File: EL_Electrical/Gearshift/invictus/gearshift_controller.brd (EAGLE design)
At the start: 69.5 x 68.4 mm, 69 parts, among them IC1 MCP2562-E_SN, IC2 MCP2515-I_SO, Q1 BSS138, Q10 BSS138, Q2 BSS138, Q3 BSS138, Q4 BSS138, Q5 BSS138, Q6 BSS138, Q8 BSS138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

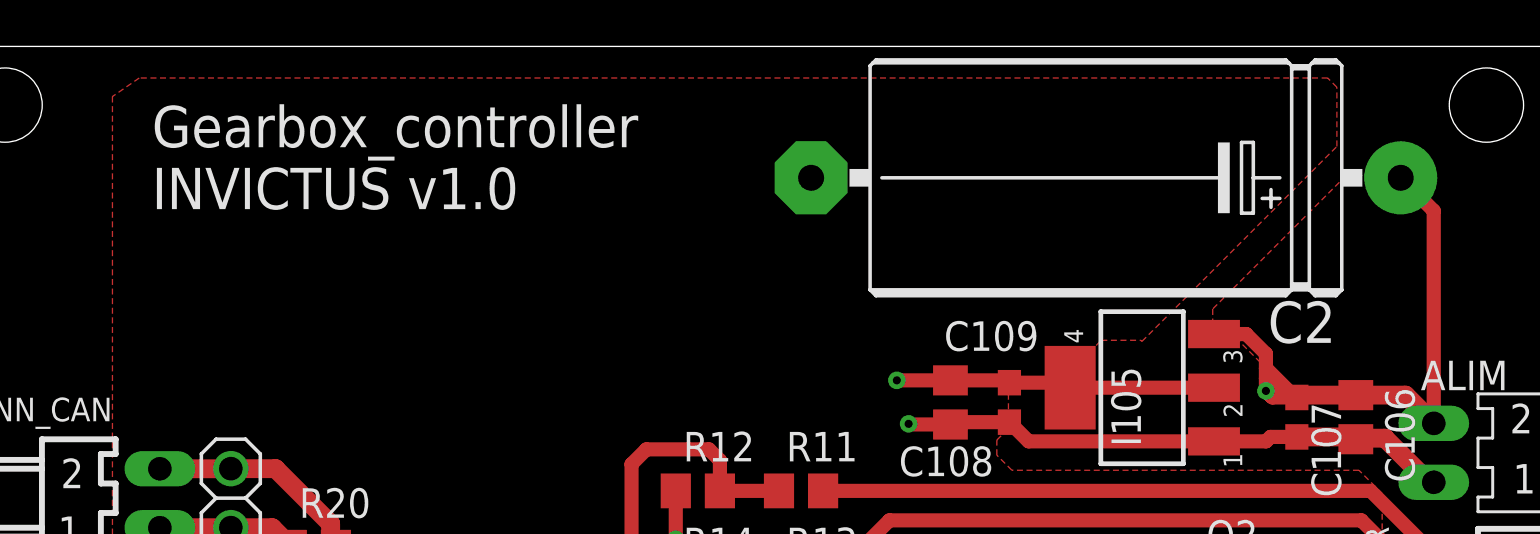
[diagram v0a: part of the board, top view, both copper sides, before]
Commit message: Delete useless resistors (Dashboard_controller)
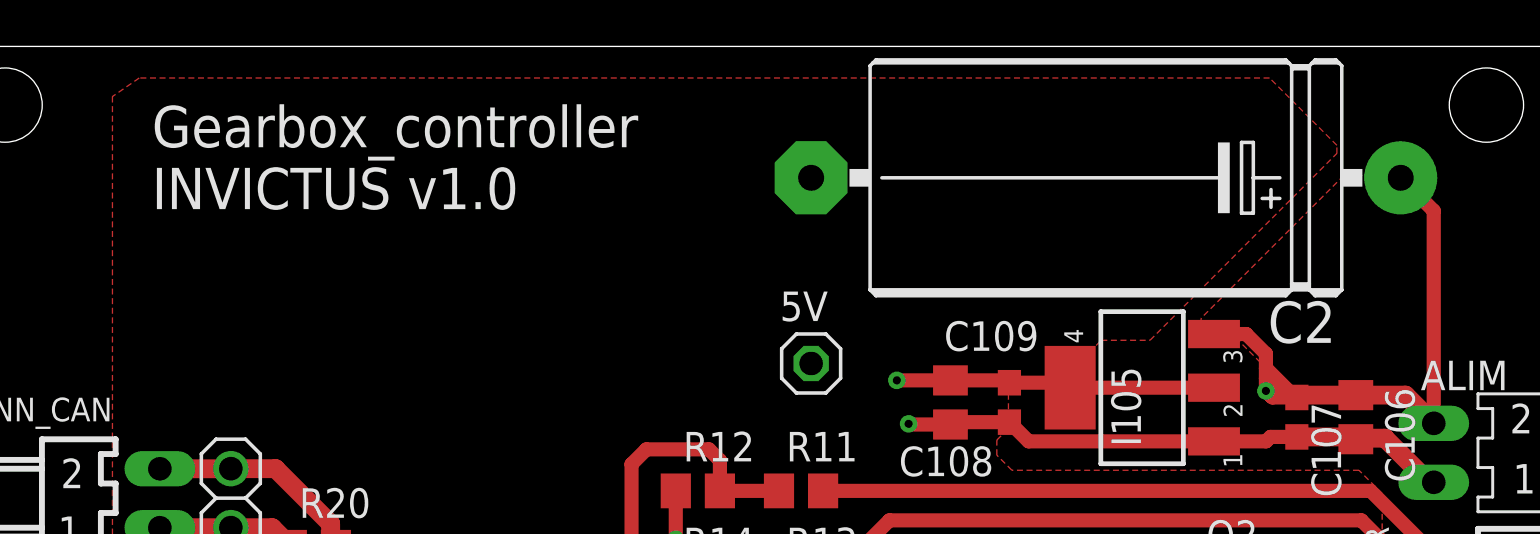
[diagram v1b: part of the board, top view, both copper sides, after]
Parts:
- added 5V: (no value), pinhead:1X01
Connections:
- net +5V: now also 5V.1
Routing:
- net +5V: track 133.2 -> 137.4 mm
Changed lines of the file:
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@@
 <setting verticaltext="up"/>
 </settings>
-<grid distance="0.05" unitdist="mm" unit="mm" style="lines" multiple="1" display="no" altdistance="0.1" altunitdist="mm" altunit="mm"/>
+<grid distance="0.1" unitdist="mm" unit="mm" style="lines" multiple="1" display="no" altdistance="0.1" altunitdist="mm" altunit="mm"/>
 <layers>
-<layer number="1" name="Top" color="4" fill="1" visible="no" active="yes"/>
+<layer number="1" name="Top" color="4" fill="1" visible="yes" active="yes"/>
 <layer number="2" name="Route2" color="16" fill="1" visible="yes" active="yes"/>
 <layer number="3" name="Route3" color="17" fill="1" visible="no" active="no"/>
@@
 <layer number="13" name="Route13" color="21" fill="1" visible="no" active="no"/>
 <layer number="14" name="Route14" color="22" fill="1" visible="no" active="no"/>
-<layer number="15" name="Route15" color="23" fill="1" visible="no" active="yes"/>
-<layer number="16" name="Bottom" color="1" fill="1" visible="no" active="yes"/>
+<layer number="15" name="Route15" color="23" fill="1" visible="yes" active="yes"/>
+<layer number="16" name="Bottom" color="1" fill="1" visible="yes" active="yes"/>
 <layer number="17" name="Pads" color="2" fill="1" visible="yes" active="yes"/>
 <layer number="18" name="Vias" color="2" fill="1" visible="yes" active="yes"/>
@@
 <attribute name="VALUE" x="54.6386" y="65.1892" size="1.778" layer="27" ratio="10" rot="R180"/>
 </element>
+<element name="5V" library="pinhead" library_urn="urn:adsk.eagle:library:325" package="1X01" package3d_urn="urn:adsk.eagle:package:22485/2" value="" x="37.9" y="54.7" smashed="yes">
+<attribute name="NAME" x="36.5538" y="56.5288" size="1.27" layer="25" ratio="10"/>
+<attribute name="POPULARITY" value="64" x="37.9" y="54.7" size="1.778" layer="27" display="off"/>
+<attribute name="VALUE" x="36.63" y="51.525" size="1.27" layer="27"/>
+</element>
 </elements>
 <signals>
@@
 <polygon width="0.6096" layer="1">
 <vertex x="63.3" y="62.8"/>
-<vertex x="60.95" y="62.8"/>
-<vertex x="55.2" y="57.05"/>
-<vertex x="55.2" y="56.1"/>
+<vertex x="60.85" y="62.8"/>
+<vertex x="54.7" y="56.65"/>
+<vertex x="54.7" y="56.1"/>
 <vertex x="55.9" y="56.1"/>
 <vertex x="57.5" y="54.5"/>
@@
 <vertex x="49.3" y="54.6"/>
 <vertex x="50.4" y="55.7"/>
-<vertex x="52.1" y="55.7"/>
-<vertex x="52.15" y="55.65"/>
-<vertex x="60.55" y="64.05"/>
-<vertex x="60.55" y="66.6"/>
-<vertex x="60.15" y="67"/>
+<vertex x="52.5" y="55.7"/>
+<vertex x="60.55" y="63.75"/>
+<vertex x="60.55" y="64.1"/>
+<vertex x="57.65" y="67"/>
 <vertex x="8.9555625" y="67"/>
 </polygon>
@@
 <vertex x="55.758803125" y="25.5"/>
 </polygon>
-<wire x1="54.2925" y1="20.32" x2="54.3075" y2="20.34" width="0" layer="19" extent="1-2"/>
-<wire x1="55.7325" y1="20.64" x2="54.3075" y2="20.34" width="0" layer="19" extent="1-2"/>
+<wire x1="54.2925" y1="20.64" x2="55.7325" y2="20.64" width="0" layer="19" extent="1-1"/>
 <wire x1="55.7325" y1="11.75" x2="54.2925" y2="11.75" width="0" layer="19" extent="1-1"/>
 <wire x1="55.7325" y1="7.305" x2="54.2925" y2="7.305" width="0" layer="19" extent="1-1"/>
@@
 <wire x1="52.3875" y1="11.75" x2="54.2925" y2="11.75" width="0" layer="19" extent="1-1"/>
 <wire x1="52.3875" y1="7.305" x2="54.2925" y2="7.305" width="0" layer="19" extent="1-1"/>
-<wire x1="60.6" y1="8.4" x2="55.7325" y2="7.305" width="0" layer="19" extent="1-1"/>
-<wire x1="33.02" y1="7.3025" x2="52.3875" y2="7.305" width="0" layer="19" extent="1-16"/>
 </signal>
 <signal name="IN0_3.3V">
@@
 <vertex x="62.2" y="26.9"/>
 <vertex x="62.5" y="27.2"/>
-<vertex x="62.5" y="65.9"/>
-<vertex x="61.3" y="67.1"/>
+<vertex x="62.5" y="59.4"/>
+<vertex x="54.8" y="67.1"/>
 <vertex x="6.7" y="67.1"/>
 <vertex x="6.7" y="39.6"/>
@@
 <vertex x="8" y="24.2"/>
 </polygon>
+<contactref element="5V" pad="1"/>
+<wire x1="37.9" y1="54.7" x2="41.3" y2="54.7" width="0.6096" layer="15"/>
+<wire x1="41.5925" y1="54.4075" x2="41.5925" y2="53.975" width="0.6096" layer="15"/>
+<wire x1="41.3" y1="54.7" x2="41.5925" y2="54.4075" width="0.6096" layer="15"/>
 <wire x1="60.6425" y1="28.255" x2="60.1675" y2="28.575" width="0" layer="19" extent="1-1"/>
 </signal>

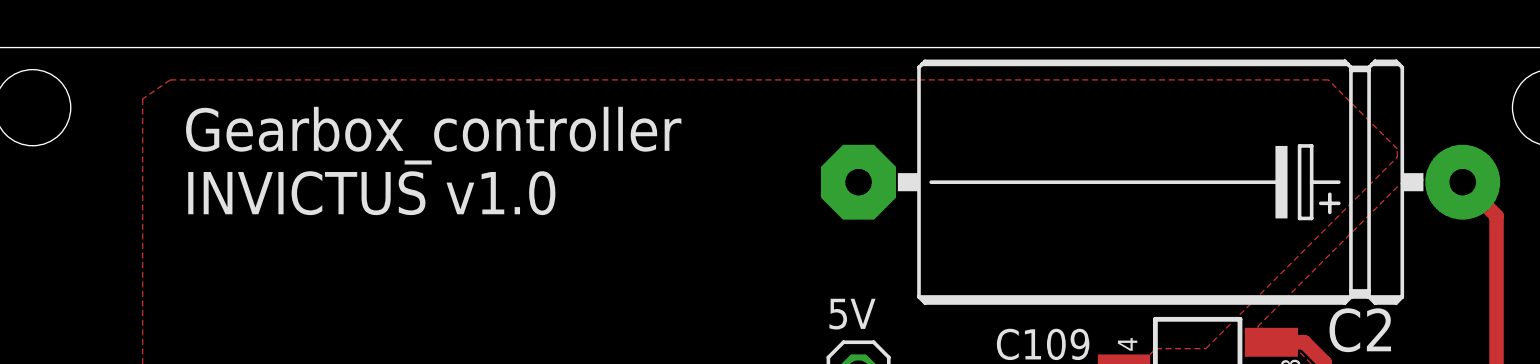
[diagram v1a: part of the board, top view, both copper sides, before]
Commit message: Delete useless resistors (Dashboard_controller)
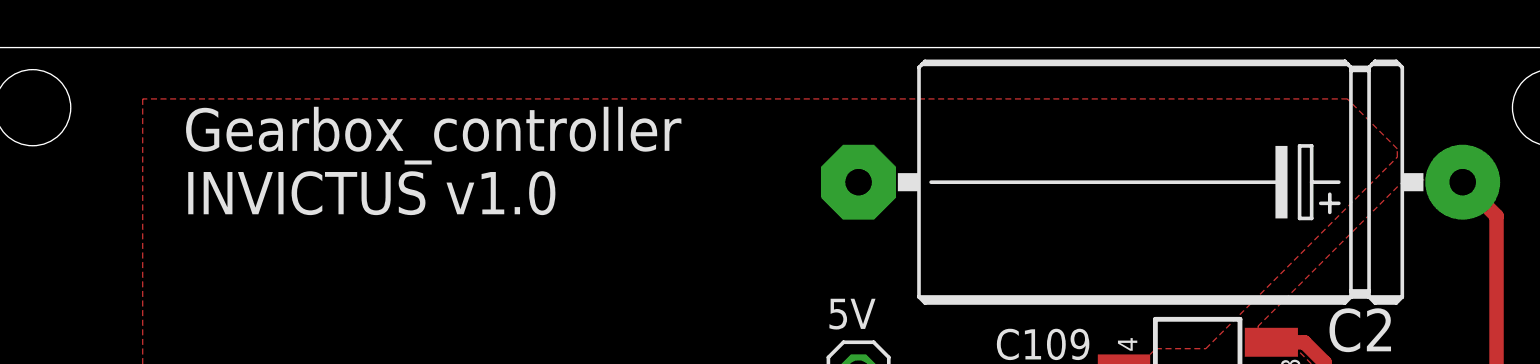
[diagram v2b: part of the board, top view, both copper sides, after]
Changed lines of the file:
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@@
 <vertex x="60.55" y="63.75"/>
 <vertex x="60.55" y="64.1"/>
-<vertex x="57.65" y="67"/>
-<vertex x="8.9555625" y="67"/>
+<vertex x="58.450003125" y="66.199996875"/>
 </polygon>
 <polygon width="0.6096" layer="2">

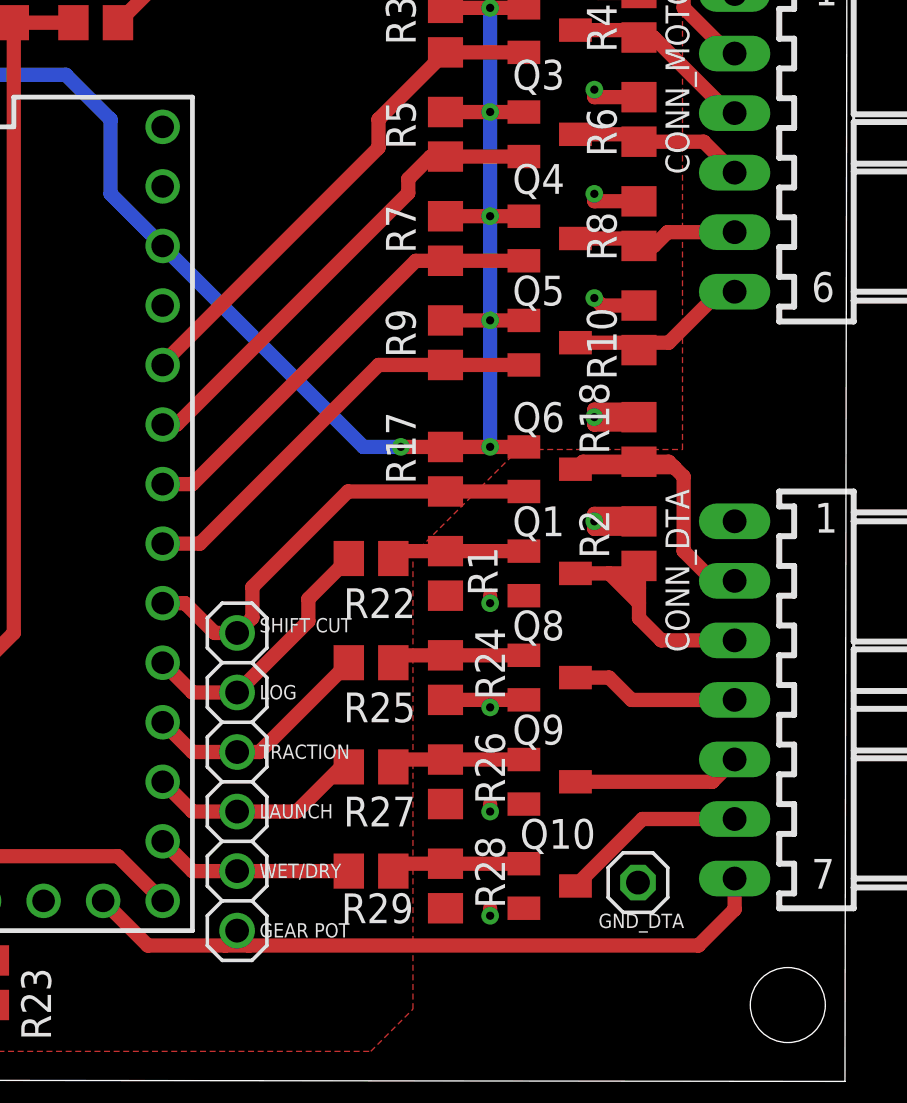
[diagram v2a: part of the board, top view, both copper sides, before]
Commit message: Add neutral sensor connector (to use with Teensy's pull-up resistors), delete uselless dta test pins
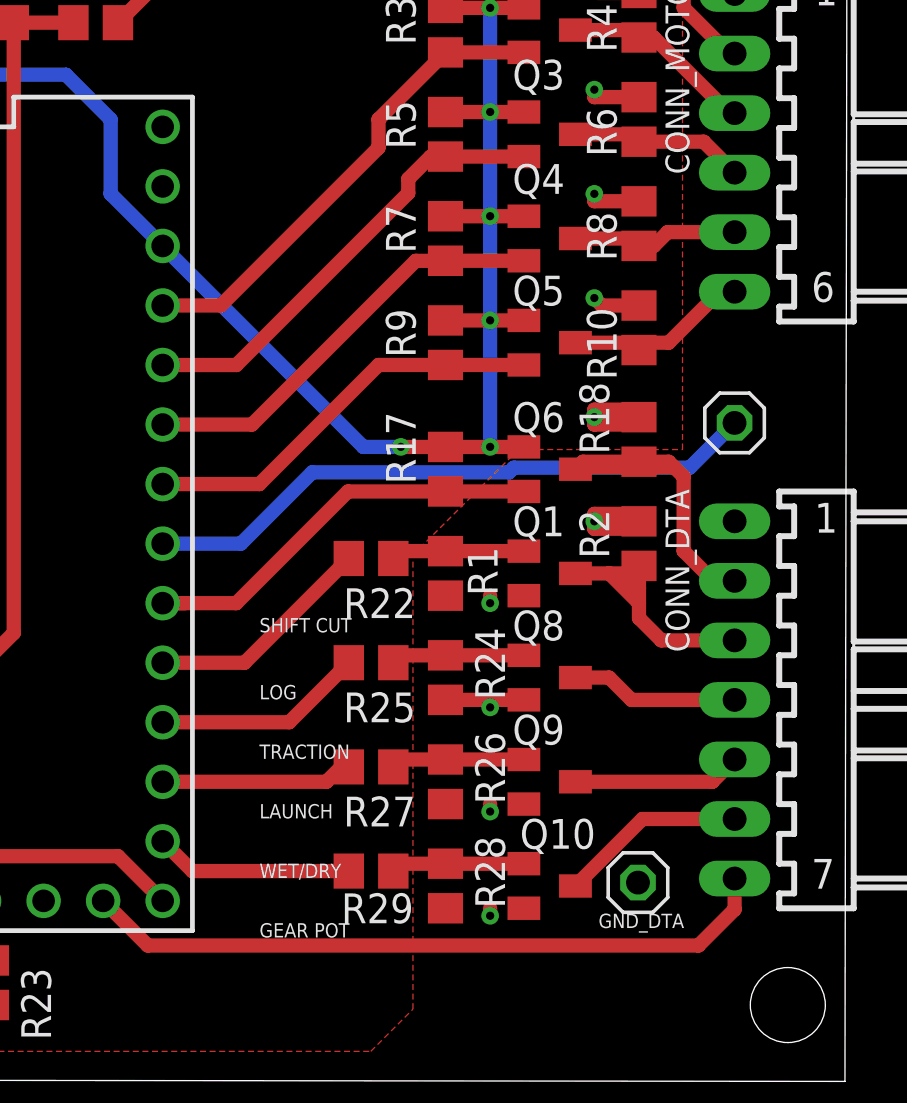
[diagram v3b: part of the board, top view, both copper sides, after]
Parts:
- removed TEST_DTA: (no value), test_pin_DTA:1X06
- added SENSOR_NEUTRE: (no value), pinhead:1X01
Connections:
- new net SENSOR_NEUTRE: SENSOR_NEUTRE.1, U$1.19/A5
- net GEAR_POT: no longer TEST_DTA.6
- net LAUNCH_CONTROL_3.3V: no longer TEST_DTA.4
- net LOG_3.3V: no longer TEST_DTA.2
- net OUT1_3.3V: now also U$1.23/A9; no longer U$1.22/A8
- net OUT2_3.3V: now also U$1.22/A8; no longer U$1.21/A7
- net OUT3_3.3V: now also U$1.21/A7; no longer U$1.20/A6
- net OUT4_3.3V: now also U$1.20/A6; no longer U$1.19/A5
- net SHIFT_CUT_3.3V: no longer TEST_DTA.1
- net TRACTION_CONTROL_3.3V: no longer TEST_DTA.3
- net WET/DRY_3.3V: no longer TEST_DTA.5
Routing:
- net SENSOR_NEUTRE: track 0.00 -> 26.5 mm
- net GEAR_POT: track 31.4 -> 29.7 mm
- net LOG_3.3V: track 11.4 -> 9.78 mm
- net OUT1_3.3V: track 21.7 -> 20.6 mm
- net TRACTION_CONTROL_3.3V: track 10.0 -> 8.99 mm
- net OUT4_3.3V: track 18.7 -> 17.6 mm
- net OUT3_3.3V: track 19.6 -> 18.6 mm
- net OUT2_3.3V: track 20.5 -> 19.4 mm
- net LAUNCH_CONTROL_3.3V: track 9.26 -> 8.20 mm
- net SHIFT_CUT_3.3V: track 19.2 -> 18.3 mm
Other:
- board text added: "SENSOR NEUTRE"

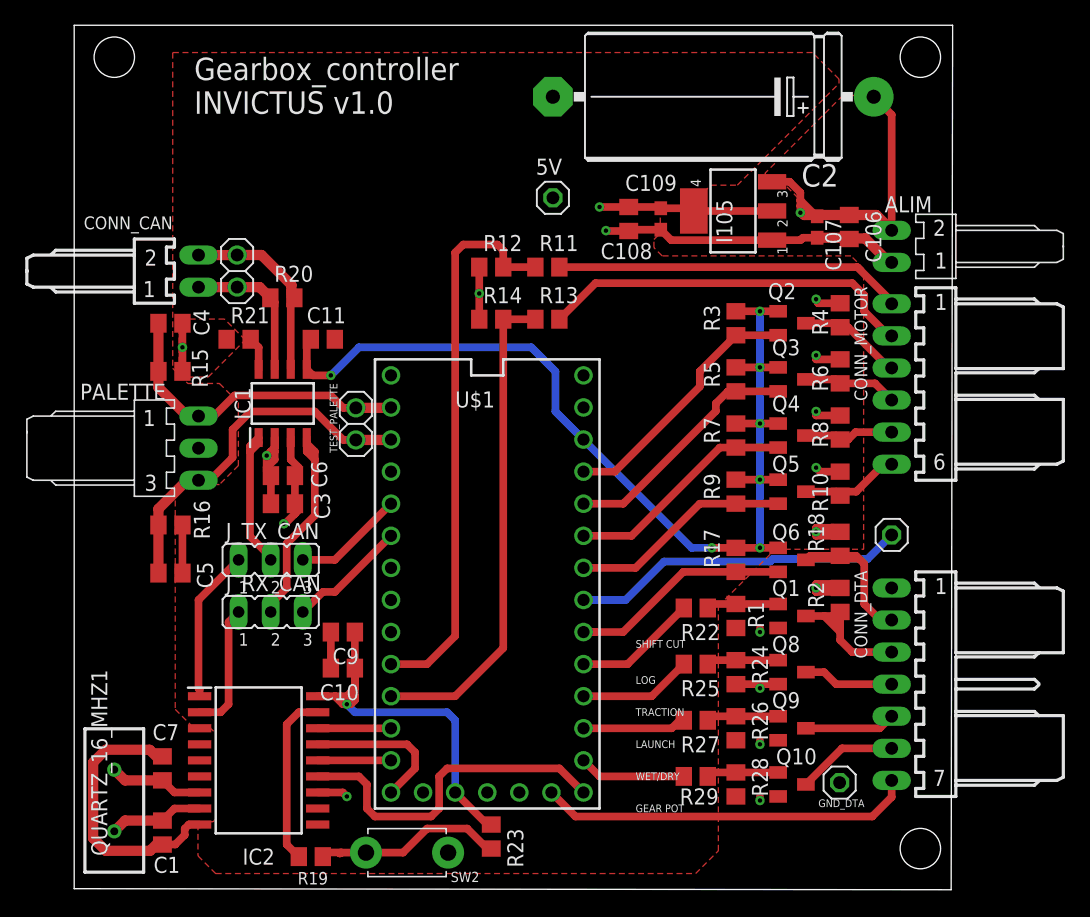
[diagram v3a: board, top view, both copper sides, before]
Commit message: Change connector footprint, LDO regulator (DC linear voltage regulator) position and reduce the size for Gearshift Controller pcb Reduce 1mm for Dashboard Controller pcb
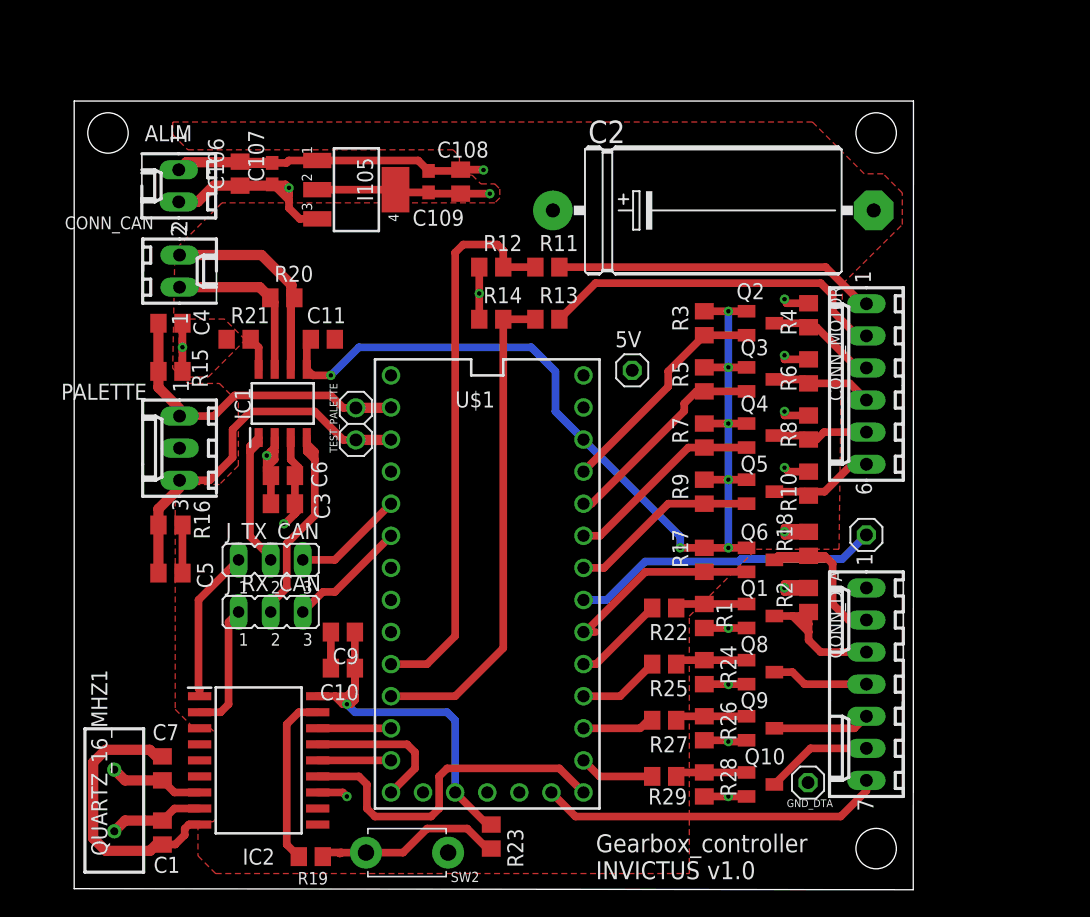
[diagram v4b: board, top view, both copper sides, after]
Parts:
- removed TEST_CAN: (no value), test_pin_DTA:1X02
- ALIM: value 22-05-7028-02 -> 22-27-2021-02; device EP_molex_6410_7395:7395-02 -> con-molex:6410-02
- CONN_CAN: value 22-05-7028-02 -> 22-27-2021-02; device con-molex:7395-02 -> con-molex:6410-02
- CONN_DTA: value 22-05-7078-07 -> 22-27-2071-07; device con-molex:7395-07 -> con-molex:6410-07
- CONN_MOTOR: value 22-05-7068-06 -> 22-27-2061-06; device con-molex:7395-06 -> con-molex:6410-06
- PALETTE: value 22-05-7038-03 -> 22-27-2031-03; device EP_molex_6410_7395:7395-03 -> con-molex:6410-03
- moved ALIM 56.6 mm to (8.28, 55.6), turned to 90 degrees
- moved C106 48.4 mm to (13.1, 56.6), turned to 90 degrees
- moved C107 43.4 mm to (15.7, 56.6), turned to 90 degrees
- moved I105 29.9 mm to (22.3, 55.3), turned to 270 degrees
- moved C109 18.6 mm to (28.1, 56.0), turned to 270 degrees
- moved 5V 15.0 mm to (44.2, 41.0)
- moved C108 13.6 mm to (30.6, 56.0), turned to 90 degrees
- moved C2 9.00 mm to (50.6, 53.7), turned to 0 degrees
- moved GND_DTA 2.50 mm to (58.1, 8.40)
- moved Q1 2.50 mm to (54.3, 21.6)
- moved Q10 2.50 mm to (54.3, 8.26)
- moved Q2 2.50 mm to (54.3, 44.8)
- moved Q3 2.50 mm to (54.3, 40.3)
- moved Q4 2.50 mm to (54.3, 35.9)
- moved Q5 2.50 mm to (54.3, 31.4)
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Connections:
- net N$4: no longer TEST_CAN.1
- net N$6: no longer TEST_CAN.2
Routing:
- net +12V: track 57.1 -> 94.9 mm
- net GND: track 100.1 -> 117.2 mm
- net +5V: track 137.4 -> 122.2 mm
- net N$6: track 15.1 -> 22.1 mm
- net WET/DRY_3.3V: track 8.47 -> 5.97 mm
- net TRACTION_CONTROL_3.3V: track 8.99 -> 6.49 mm
- net SHIFT_CUT_3.3V: track 18.3 -> 15.8 mm
- net OUT4_3.3V: track 17.6 -> 15.1 mm
- net OUT3_3.3V: track 18.6 -> 16.1 mm
- net OUT2_3.3V: track 19.4 -> 16.9 mm
- net LOG_3.3V: track 9.78 -> 7.28 mm
- net LAUNCH_CONTROL_3.3V: track 8.20 -> 5.70 mm
- net OUT1_3.3V: track 20.6 -> 18.1 mm
- net GEAR_POT: track 29.7 -> 27.4 mm
- net IN0_12V: track 27.6 -> 25.5 mm
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- removed copper zone on layer 1, net +12V
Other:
- board size 69.5 x 68.4 mm -> 66.4 x 62.4 mm
